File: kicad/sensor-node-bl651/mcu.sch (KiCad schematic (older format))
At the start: 15 parts, among them U1 DMP2008UFG-7, Y1 32.768 kHz

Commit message: remove fuses
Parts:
- removed F3: Polyfuse, Fuse:Fuse_0603_1608Metric, symbol Device:Polyfuse
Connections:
- wire segments 71 -> 70
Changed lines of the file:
@@
 NoConn ~ 6600 3250
-$Comp
-L Device:Polyfuse F3
-U 1 1 601D34D6
-P 8600 6250
-F 0 "F3" V 8375 6250 50  0000 C CNN
-F 1 "Polyfuse" V 8466 6250 50  0000 C CNN
-F 2 "Fuse:Fuse_0603_1608Metric" H 8650 6050 50  0001 L CNN
-F 3 "https://belfuse.com/resources/datasheets/circuitprotection/ds-cp-0zcm-series.pdf" H 8600 6250 50  0001 C CNN
-F 4 "507-0ZCM0002FF2GCT-ND" V 8600 6250 50  0001 C CNN "Digi-Key Part Number"
-F 5 "Bel Fuse Inc." V 8600 6250 50  0001 C CNN "Manufacturer"
-F 6 "0ZCM0002FF2G" V 8600 6250 50  0001 C CNN "Manufacturer Part Number"
-F 7 "PTC RESET FUSE 60V 20MA 0603" V 8600 6250 50  0001 C CNN "Description"
-	1    8600 6250
-	0    1    1    0
-$EndComp
 $Comp
 L HH_DiodesIncorporated:DMP2008UFG-7 U1
@@
 Wire Wire Line
 	8400 5700 9300 5700
-Wire Wire Line
-	8300 6250 8450 6250
 Connection ~ 8300 6250
-Wire Wire Line
-	8750 6250 8900 6250
 NoConn ~ 6600 3050
 NoConn ~ 6600 2250
@@
 	1650 4850 1150 4850
 NoConn ~ 4800 3650
+Wire Wire Line
+	8300 6250 8900 6250
 $EndSCHEMATC

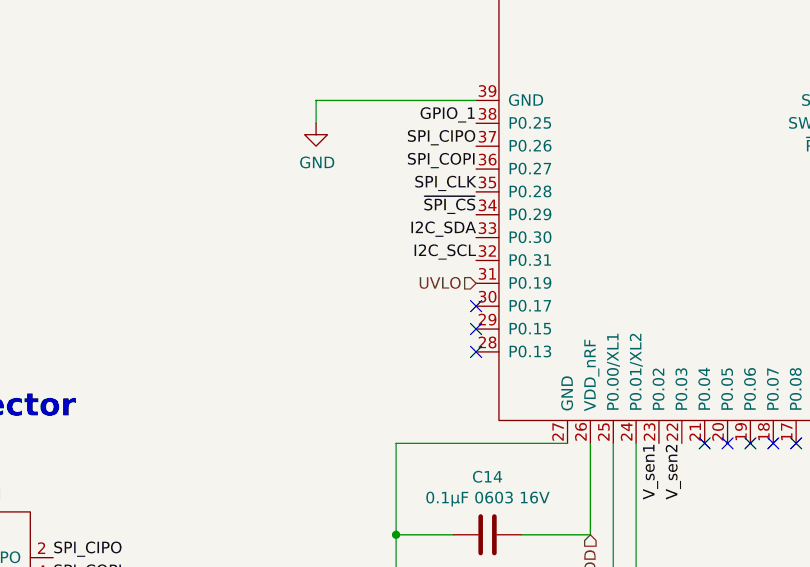
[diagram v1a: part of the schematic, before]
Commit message: add TPS6031x
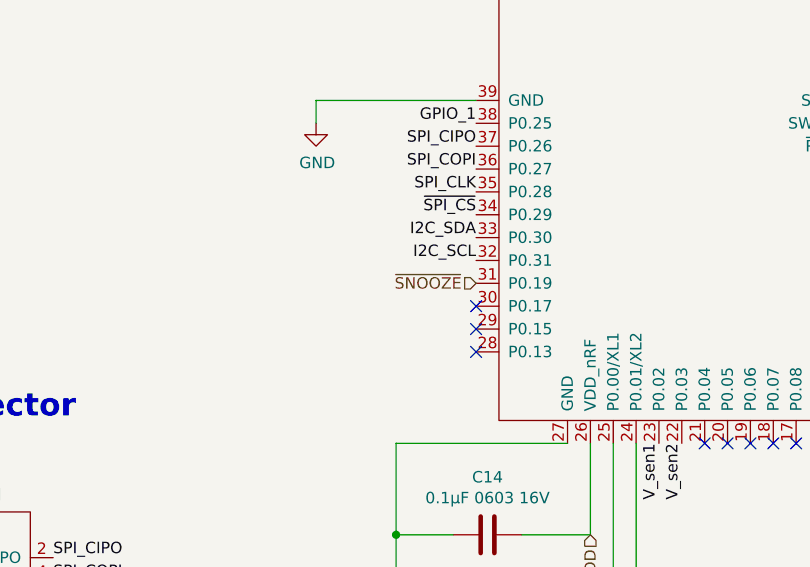
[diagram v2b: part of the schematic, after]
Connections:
- net UVLO renamed ~SNOOZE
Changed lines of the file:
@@
 NoConn ~ 6600 2950
 Text HLabel 4800 3350 0    50   Input ~ 0
-UVLO
+~SNOOZE
 $Comp
 L HH_Hochreiner:swd_connector S2

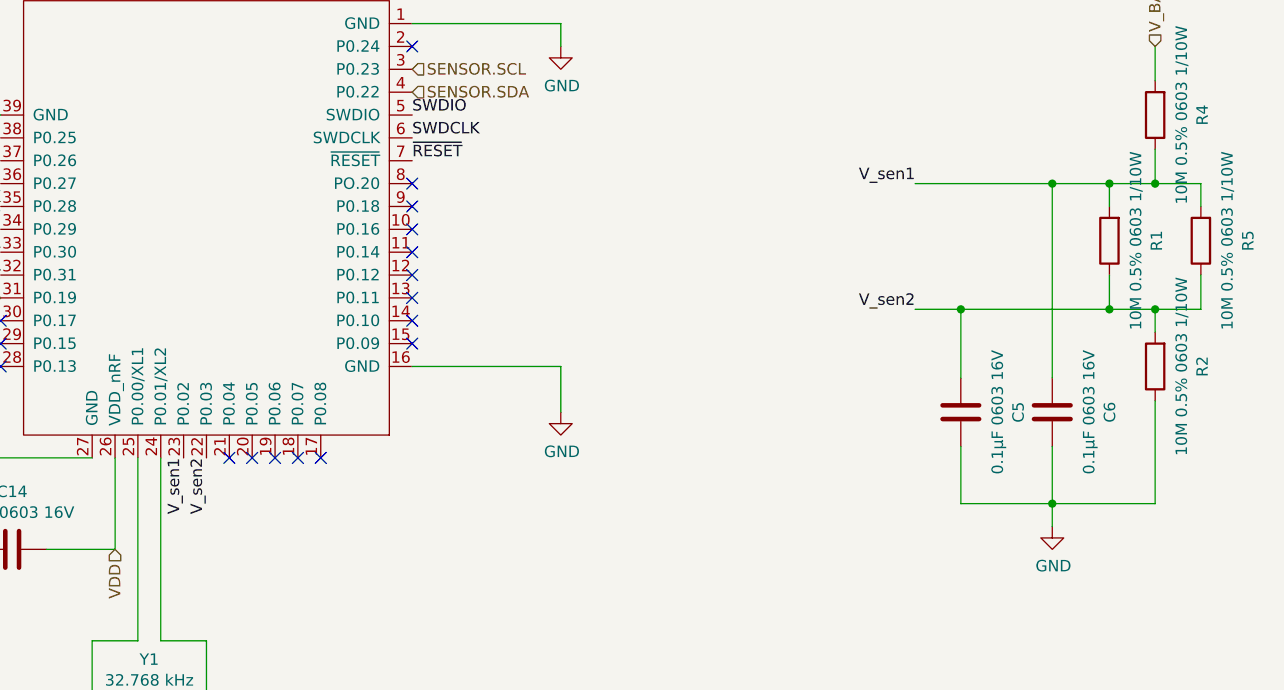
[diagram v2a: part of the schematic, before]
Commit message: remove second measurement point
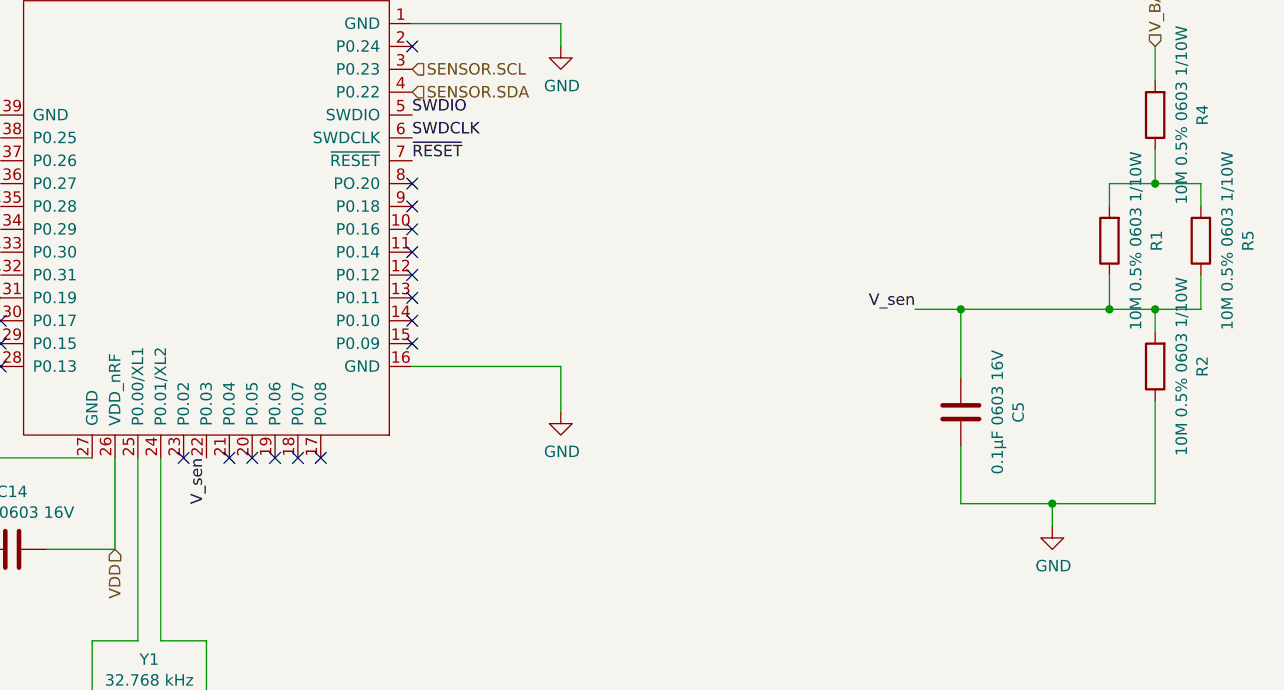
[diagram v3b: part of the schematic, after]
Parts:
- removed C6: 0.1µF 0603 16V, Capacitor_SMD:C_0603_1608Metric, symbol Device:C
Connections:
- net V_sen1: no longer names the net of R1.2, R4.1, R5.2
- net V_sen1: no longer BL1.23 (P0.02)
- net V_sen2 renamed V_sen
- no-connect marks 17 -> 18
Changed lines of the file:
@@
 Wire Wire Line
 	9850 2400 9850 2250
-Text Label 8800 2850 2    50   ~ 0
-V_sen1
 Text Label 8800 3400 2    50   ~ 0
-V_sen2
-Connection ~ 9650 2850
+V_sen
 Connection ~ 9650 3400
 Text Label 5700 4050 3    50   ~ 0
-V_sen2
-Text Label 5600 4050 3    50   ~ 0
-V_sen1
-$Comp
-L Device:C C6
-U 1 1 6021C849
-P 9400 3850
-F 0 "C6" V 9148 3850 50  0000 C CNN
-F 1 "0.1µF 0603 16V" V 9239 3850 50  0000 C CNN
-F 2 "Capacitor_SMD:C_0603_1608Metric" H 9438 3700 50  0001 C CNN
-F 3 "~" H 9400 3850 50  0001 C CNN
-	1    9400 3850
-	-1   0    0    1
-$EndComp
+V_sen
 $Comp
 L Device:C C5
@@
 	8800 3400 9000 3400
 Wire Wire Line
-	8800 2850 9400 2850
-Wire Wire Line
-	9400 3700 9400 2850
-Connection ~ 9400 2850
-Wire Wire Line
-	9400 2850 9650 2850
-Wire Wire Line
 	9000 3700 9000 3400
 Connection ~ 9000 3400
@@
 	9850 3800 9850 4250
 Connection ~ 9400 4250
-Wire Wire Line
-	9400 4250 9400 4000
 Wire Wire Line
 	9400 4250 9000 4250
@@
 Wire Wire Line
 	8300 6250 8900 6250
+NoConn ~ 5600 4050
 $EndSCHEMATC

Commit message: update swd footprint
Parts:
- S2: footprint HH_Hochreiner:swd_connector -> HH_Hochreiner:SWD_BD050-06-A-0-0500-L-D; Description CONN RCPT 6POS 0.05 GOLD SMD -> 6W,1.27MM SOCKET,DIL, SMT,L/PROF; Digi-Key Part Number SAM10974-ND -> 2073-BD050-06-A-0-0500-L-D-ND; Manufacturer Samtec Inc. -> GCT; Manufacturer Part Number CLP-103-02-G-D-BE -> BD050-06-A-0-0500-L-D
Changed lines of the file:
@@
 F 0 "S2" H 9900 6165 50  0000 C CNN
 F 1 "swd_connector" H 9900 6074 50  0000 C CNN
-F 2 "HH_Hochreiner:swd_connector" H 9900 5800 50  0001 C CNN
-F 3 "http://suddendocs.samtec.com/catalog_english/clp_sm.pdf" H 9900 5800 50  0001 C CNN
-F 4 "SAM10974-ND" H 9900 5800 50  0001 C CNN "Digi-Key Part Number"
-F 5 "Samtec Inc." H 9900 5800 50  0001 C CNN "Manufacturer"
-F 6 "CLP-103-02-G-D-BE" H 9900 5800 50  0001 C CNN "Manufacturer Part Number"
-F 7 "CONN RCPT 6POS 0.05 GOLD SMD" H 9900 5800 50  0001 C CNN "Description"
+F 2 "HH_Hochreiner:SWD_BD050-06-A-0-0500-L-D" H 9900 5800 50  0001 C CNN
+F 3 "https://gct.co/files/drawings/bd050.pdf" H 9900 5800 50  0001 C CNN
+F 4 "2073-BD050-06-A-0-0500-L-D-ND" H 9900 5800 50  0001 C CNN "Digi-Key Part Number"
+F 5 "GCT" H 9900 5800 50  0001 C CNN "Manufacturer"
+F 6 "BD050-06-A-0-0500-L-D" H 9900 5800 50  0001 C CNN "Manufacturer Part Number"
+F 7 "6W,1.27MM SOCKET,DIL, SMT,L/PROF" H 9900 5800 50  0001 C CNN "Description"
 	1    9900 5800
 	1    0    0    -1

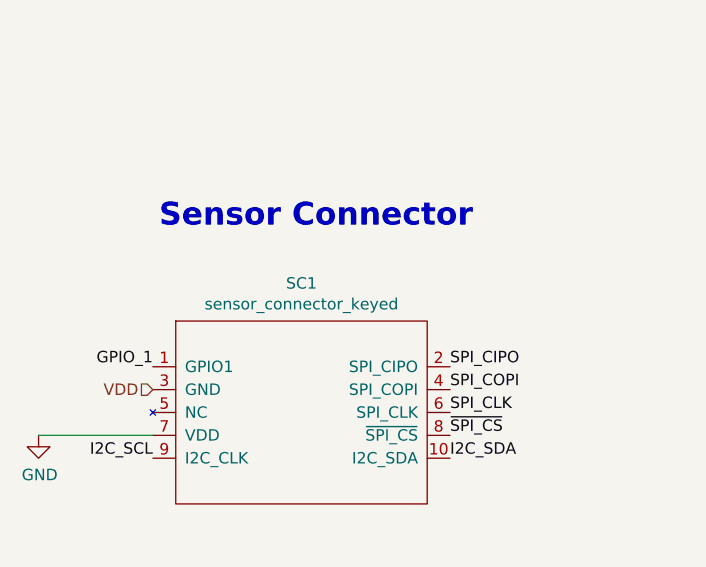
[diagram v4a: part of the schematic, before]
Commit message: update sensor connector
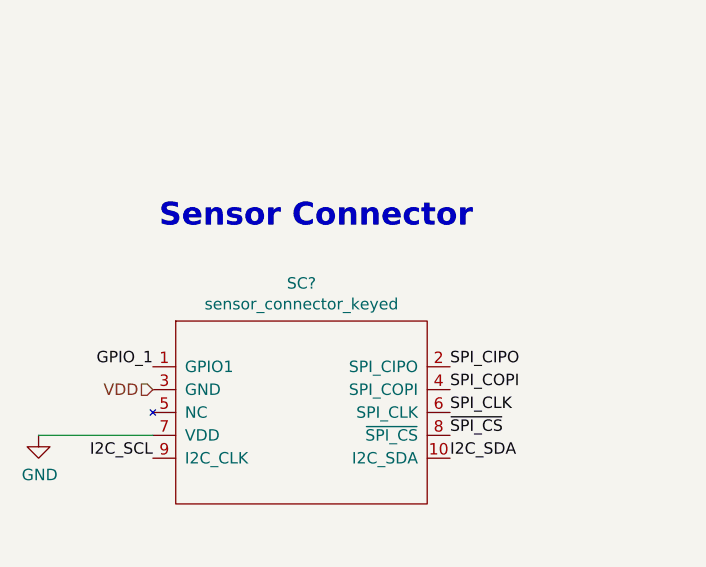
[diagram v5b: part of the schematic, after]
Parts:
- removed SC1: sensor_connector_keyed, HH_Hochreiner:sensor_connector_M50-3150542R_keyed, symbol HH_Hochreiner:sensor_connector_keyed
- added SC?: sensor_connector_keyed, HH_Hochreiner:Sensor-Connector_BD050-10-A-0-0500-L-D, symbol HH_Hochreiner:sensor_connector_keyed
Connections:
- net GND: now also SC?.7 (VDD)
- net GPIO_1: now also SC?.1 (GPIO1)
- net I2C_SCL: now also SC?.9 (I2C_CLK)
- net I2C_SDA: now also SC?.10 (I2C_SDA)
- net SPI_CIPO: now also SC?.2 (SPI_CIPO)
- net SPI_CLK: now also SC?.6 (SPI_CLK)
- net SPI_COPI: now also SC?.4 (SPI_COPI)
- net VDD: now also SC?.3 (GND)
- net ~SPI_CS: now also SC?.8 (~SPI_CS)
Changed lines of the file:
@@
-	1    0    0    -1
-$EndComp
-$Comp
-L HH_Hochreiner:sensor_connector_keyed SC1
-U 1 1 6025A1AC
-P 2300 4750
-F 0 "SC1" H 2300 5315 50  0000 C CNN
-F 1 "sensor_connector_keyed" H 2300 5224 50  0000 C CNN
-F 2 "HH_Hochreiner:sensor_connector_M50-3150542R_keyed" H 2300 4750 50  0001 C CNN
-F 3 "https://cdn.harwin.com/pdfs/C029XX_M50_and_M52_Series_Connectors.pdf" H 2300 4750 50  0001 C CNN
-F 4 "952-3493-1-ND" H 2300 4750 50  0001 C CNN "Digi-Key Part Number"
-F 5 "Harwin Inc." H 2300 4750 50  0001 C CNN "Manufacturer"
-F 6 "M50-3150542R" H 2300 4750 50  0001 C CNN "Manufacturer Part Number"
-F 7 "CONN RCPT 10POS 0.05 GOLD SMD" H 2300 4750 50  0001 C CNN "Description"
-	1    2300 4750
 	1    0    0    -1
 $EndComp
@@
 	8300 6250 8900 6250
 NoConn ~ 5600 4050
+$Comp
+L HH_Hochreiner:sensor_connector_keyed SC?
+U 1 1 60B6C2F4
+P 2300 4750
+F 0 "SC?" H 2300 5315 50  0000 C CNN
+F 1 "sensor_connector_keyed" H 2300 5224 50  0000 C CNN
+F 2 "HH_Hochreiner:Sensor-Connector_BD050-10-A-0-0500-L-D" H 2300 4750 50  0001 C CNN
+F 3 "https://cdn.harwin.com/pdfs/C029XX_M50_and_M52_Series_Connectors.pdf" H 2300 4750 50  0001 C CNN
+F 4 "2073-BD050-10-A-0-0500-L-D-ND" H 2300 4750 50  0001 C CNN "Digi-Key Part Number"
+F 5 "GCT" H 2300 4750 50  0001 C CNN "Manufacturer"
+F 6 "BD050-10-A-0-0500-L-D" H 2300 4750 50  0001 C CNN "Manufacturer Part Number"
+F 7 "10W,1.27MM SOCKET,DIL, SMT,L/PRO" H 2300 4750 50  0001 C CNN "Description"
+	1    2300 4750
+	1    0    0    -1
+$EndComp
 $EndSCHEMATC

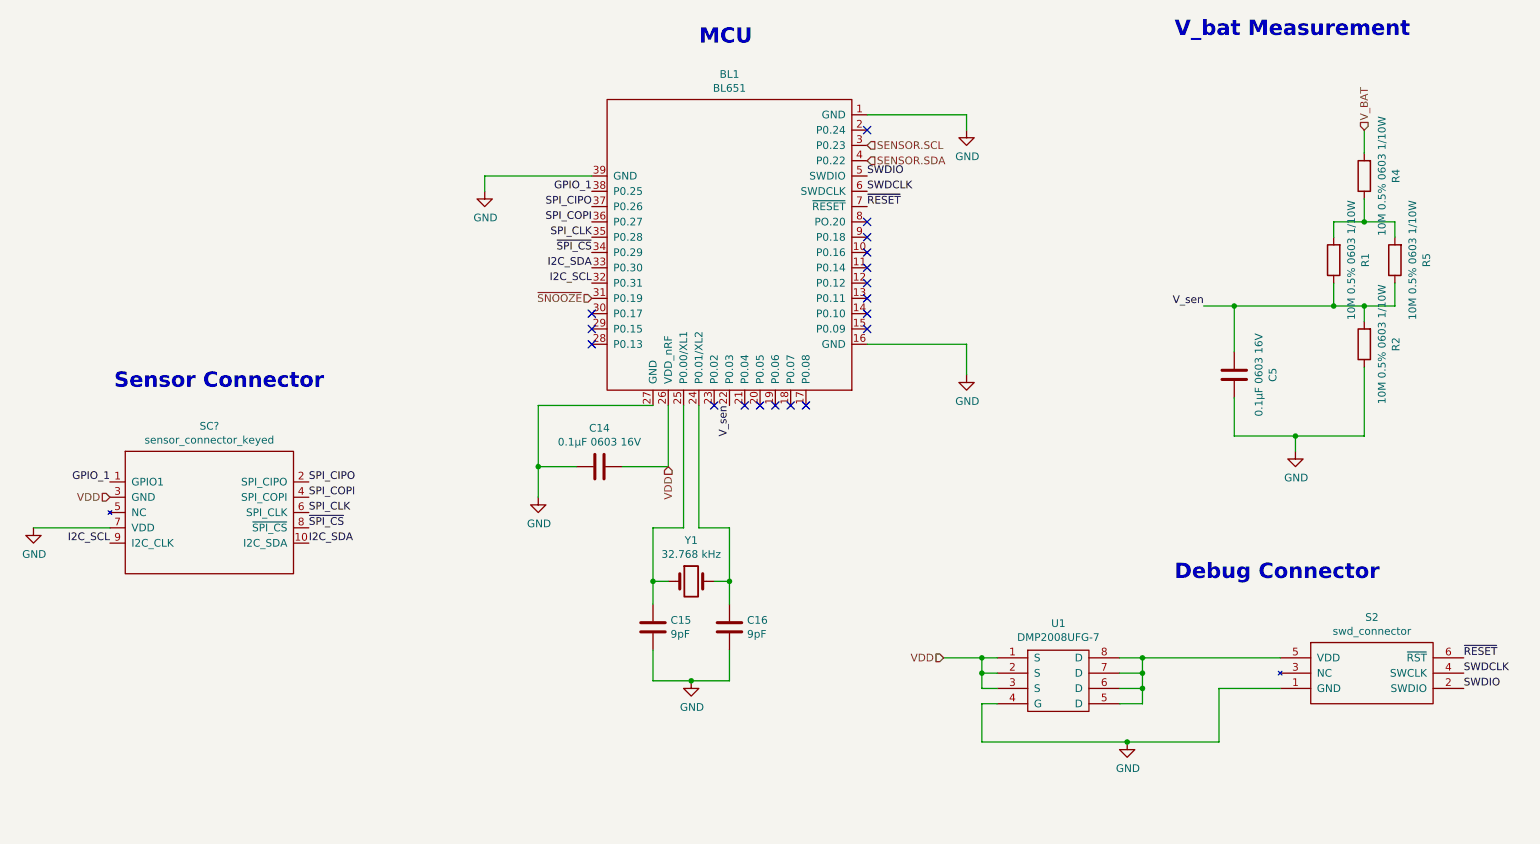
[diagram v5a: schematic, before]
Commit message: update sensor and swd connectors
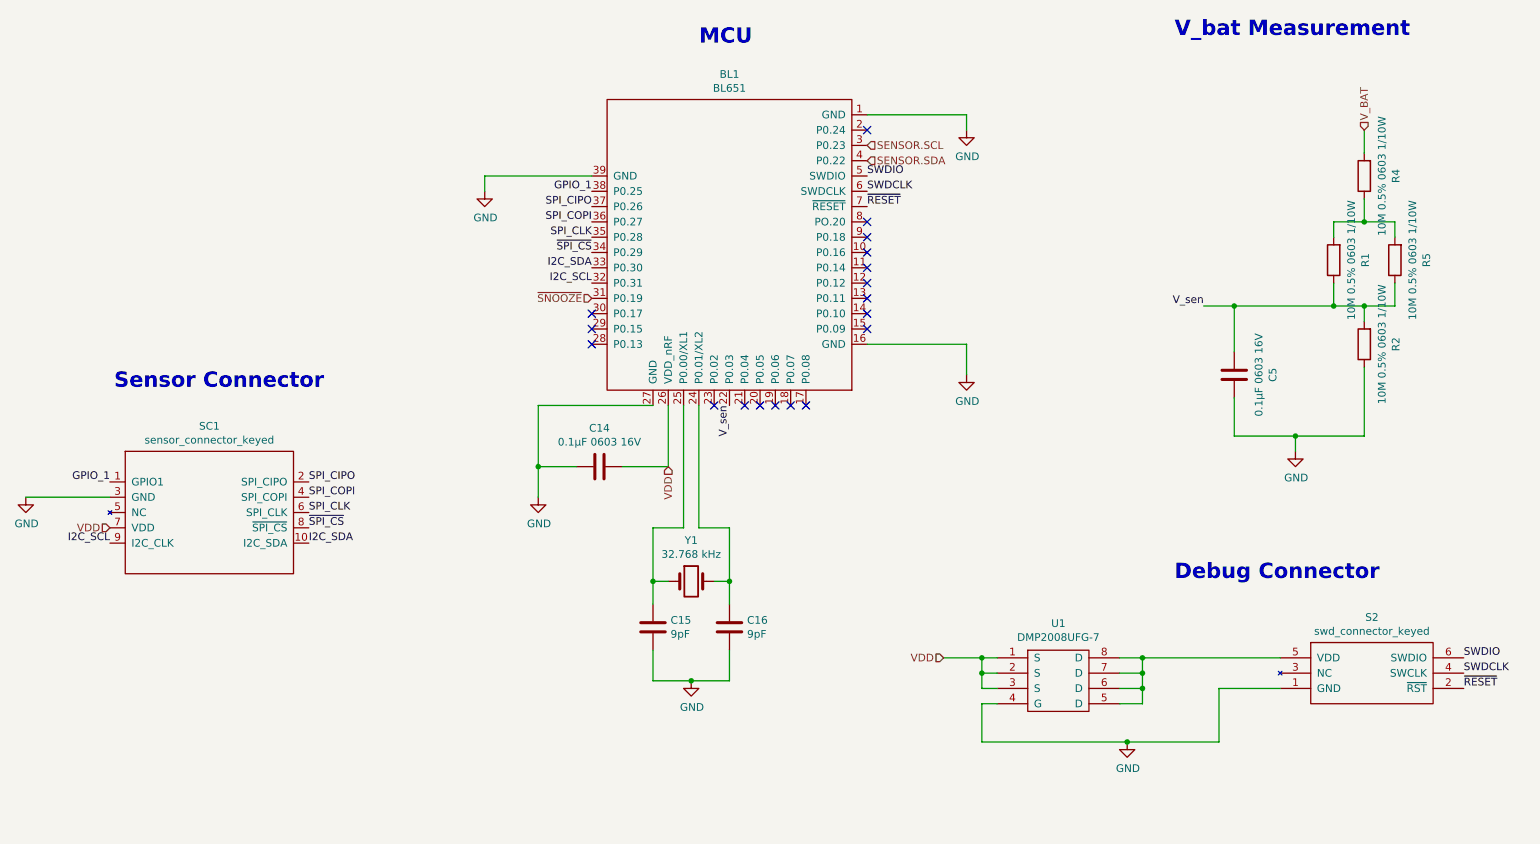
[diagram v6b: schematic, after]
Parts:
- removed S2: swd_connector, HH_Hochreiner:SWD_BD050-06-A-0-0500-L-D, symbol HH_Hochreiner:swd_connector
- removed SC?: sensor_connector_keyed, HH_Hochreiner:Sensor-Connector_BD050-10-A-0-0500-L-D, symbol HH_Hochreiner:sensor_connector_keyed
- added S2: swd_connector_keyed, HH_Hochreiner:SWD_BD050-06-A-0-0500-L-D, symbol HH_Hochreiner:swd_connector_keyed
- added SC1: sensor_connector_keyed, HH_Hochreiner:Sensor-Connector_BD050-10-A-0-0500-L-D, symbol HH_Hochreiner:sensor_connector_keyed
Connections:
- net GND: now also S2.1 (GND), SC1.3 (GND)
- net GPIO_1: now also SC1.1 (GPIO1)
- net I2C_SCL: now also SC1.9 (I2C_CLK)
- net I2C_SDA: now also SC1.10 (I2C_SDA)
- net SPI_CIPO: now also SC1.2 (SPI_CIPO)
- net SPI_CLK: now also SC1.6 (SPI_CLK)
- net SPI_COPI: now also SC1.4 (SPI_COPI)
- net SWDCLK: now also S2.4 (SWCLK)
- net SWDIO: now also S2.6 (SWDIO)
- net VDD: now also SC1.7 (VDD)
- net ~RESET: now also S2.2 (~RST)
- net ~SPI_CS: now also SC1.8 (~SPI_CS)
- net at U1.5 (D), U1.6 (D), U1.7 (D)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: now also S2.5 (VDD)
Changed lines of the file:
@@
 L power:GND #PWR0108
 U 1 1 5F904E15
-P 1150 4850
-F 0 "#PWR0108" H 1150 4600 50  0001 C CNN
-F 1 "GND" H 1155 4677 50  0000 C CNN
-F 2 "" H 1150 4850 50  0001 C CNN
-F 3 "" H 1150 4850 50  0001 C CNN
-	1    1150 4850
-	1    0    0    -1
-$EndComp
-Text HLabel 1650 4650 0    50   Input ~ 0
+P 1100 4650
+F 0 "#PWR0108" H 1100 4400 50  0001 C CNN
+F 1 "GND" H 1105 4477 50  0000 C CNN
+F 2 "" H 1100 4650 50  0001 C CNN
+F 3 "" H 1100 4650 50  0001 C CNN
+	1    1100 4650
+	1    0    0    -1
+$EndComp
+Text HLabel 1650 4850 0    50   Input ~ 0
 VDD
 Text Label 2950 4750 0    50   ~ 0
@@
 Text HLabel 7100 5700 0    50   Input ~ 0
 VDD
-Text Label 10500 5700 0    50   ~ 0
+Text Label 10500 5900 0    50   ~ 0
 ~RESET
 $Comp
@@
 Text Label 10500 5800 0    50   ~ 0
 SWDCLK
-Text Label 10500 5900 0    50   ~ 0
+Text Label 10500 5700 0    50   ~ 0
 SWDIO
 Text Notes 3050 3950 2    100  ~ 20
@@
 Text HLabel 4800 3350 0    50   Input ~ 0
 ~SNOOZE
-$Comp
-L HH_Hochreiner:swd_connector S2
-U 1 1 60246EFA
-P 9900 5800
-F 0 "S2" H 9900 6165 50  0000 C CNN
-F 1 "swd_connector" H 9900 6074 50  0000 C CNN
-F 2 "HH_Hochreiner:SWD_BD050-06-A-0-0500-L-D" H 9900 5800 50  0001 C CNN
-F 3 "https://gct.co/files/drawings/bd050.pdf" H 9900 5800 50  0001 C CNN
-F 4 "2073-BD050-06-A-0-0500-L-D-ND" H 9900 5800 50  0001 C CNN "Digi-Key Part Number"
-F 5 "GCT" H 9900 5800 50  0001 C CNN "Manufacturer"
-F 6 "BD050-06-A-0-0500-L-D" H 9900 5800 50  0001 C CNN "Manufacturer Part Number"
-F 7 "6W,1.27MM SOCKET,DIL, SMT,L/PROF" H 9900 5800 50  0001 C CNN "Description"
-	1    9900 5800
-	1    0    0    -1
-$EndComp
-Wire Wire Line
-	1650 4850 1150 4850
 NoConn ~ 4800 3650
 Wire Wire Line
 	8300 6250 8900 6250
 NoConn ~ 5600 4050
-$Comp
-L HH_Hochreiner:sensor_connector_keyed SC?
-U 1 1 60B6C2F4
+Wire Wire Line
+	1100 4650 1650 4650
+$Comp
+L HH_Hochreiner:sensor_connector_keyed SC1
+U 1 1 60B919AA
 P 2300 4750
-F 0 "SC?" H 2300 5315 50  0000 C CNN
+F 0 "SC1" H 2300 5315 50  0000 C CNN
 F 1 "sensor_connector_keyed" H 2300 5224 50  0000 C CNN
 F 2 "HH_Hochreiner:Sensor-Connector_BD050-10-A-0-0500-L-D" H 2300 4750 50  0001 C CNN
@@
 	1    0    0    -1
 $EndComp
+$Comp
+L HH_Hochreiner:swd_connector_keyed S2
+U 1 1 60B93392
+P 9900 5800
+F 0 "S2" H 9900 6165 50  0000 C CNN
+F 1 "swd_connector_keyed" H 9900 6074 50  0000 C CNN
+F 2 "HH_Hochreiner:SWD_BD050-06-A-0-0500-L-D" H 9900 5800 50  0001 C CNN
+F 3 "https://www.gct.co/files/drawings/BD050.pdf" H 9900 5800 50  0001 C CNN
+F 4 "2073-BD050-06-A-0-0500-L-D-ND" H 9900 5800 50  0001 C CNN "Digi-Key Part Number"
+F 5 "GCT" H 9900 5800 50  0001 C CNN "Manufacturer"
+F 6 "BD050-06-A-0-0500-L-D" H 9900 5800 50  0001 C CNN "Manufacturer Part Number"
+F 7 "6W,1.27MM SOCKET,DIL, SMT,L/PROF" H 9900 5800 50  0001 C CNN "Description"
+	1    9900 5800
+	1    0    0    -1
+$EndComp
